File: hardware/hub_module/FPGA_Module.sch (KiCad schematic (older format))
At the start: 1 part, among them U1 TE0714

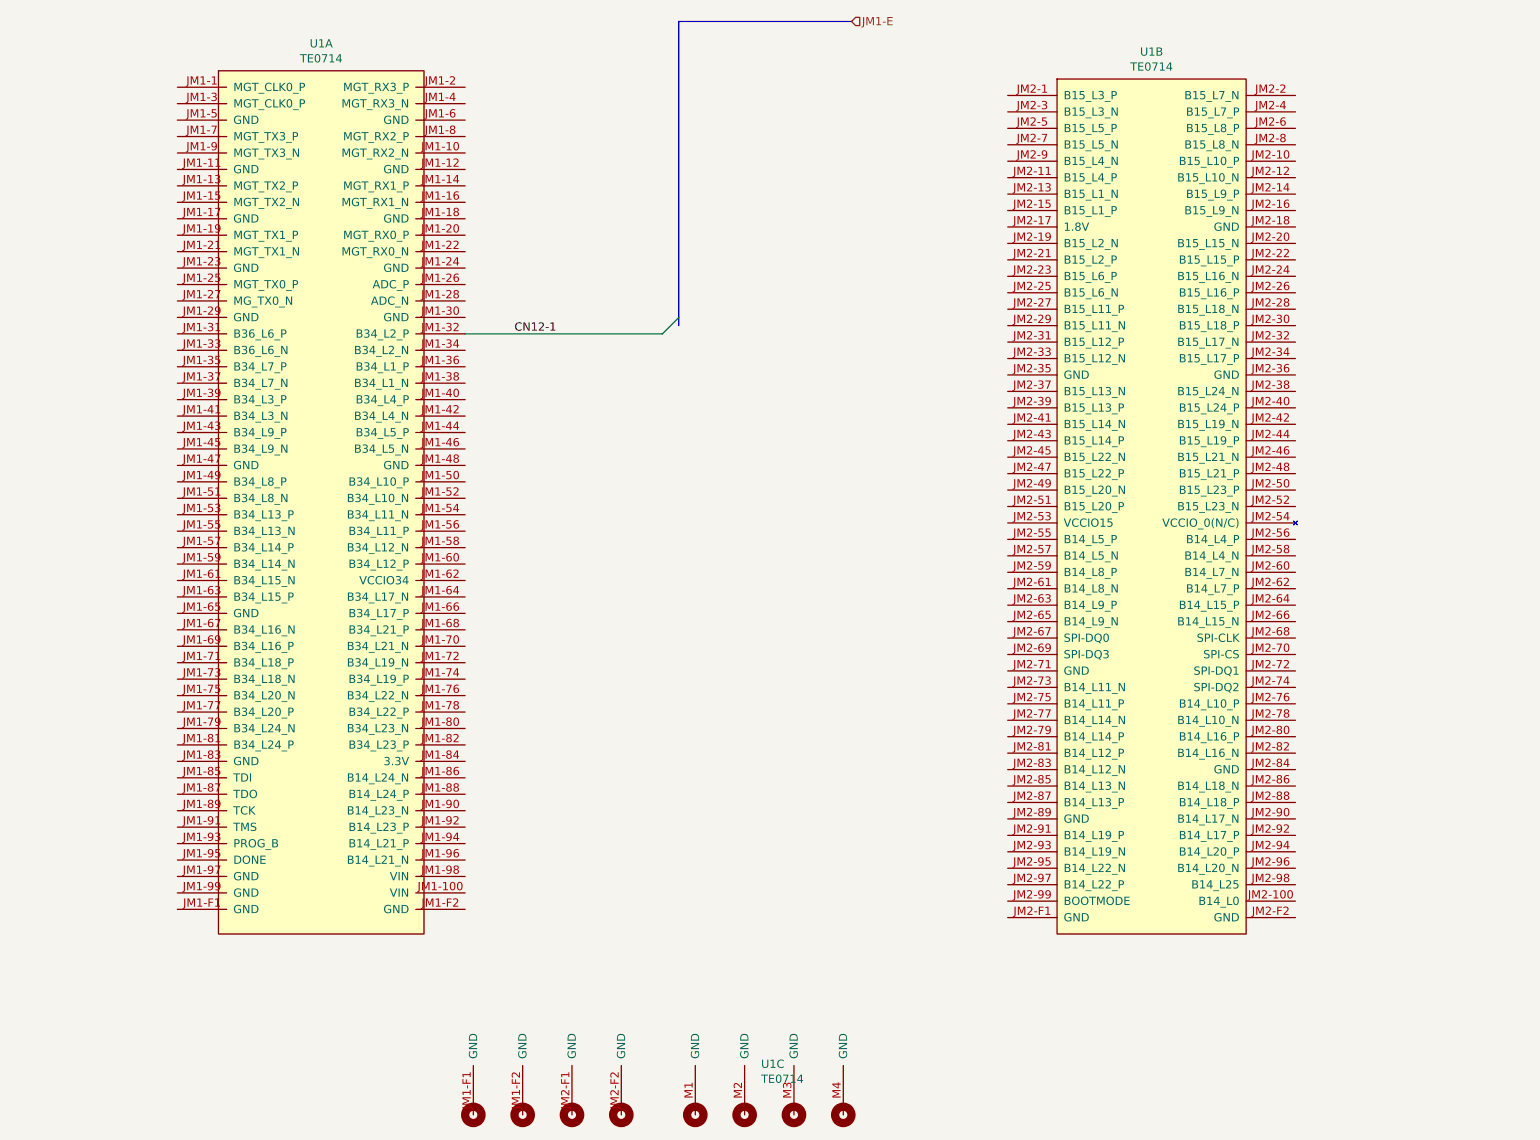
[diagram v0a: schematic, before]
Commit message: busses added
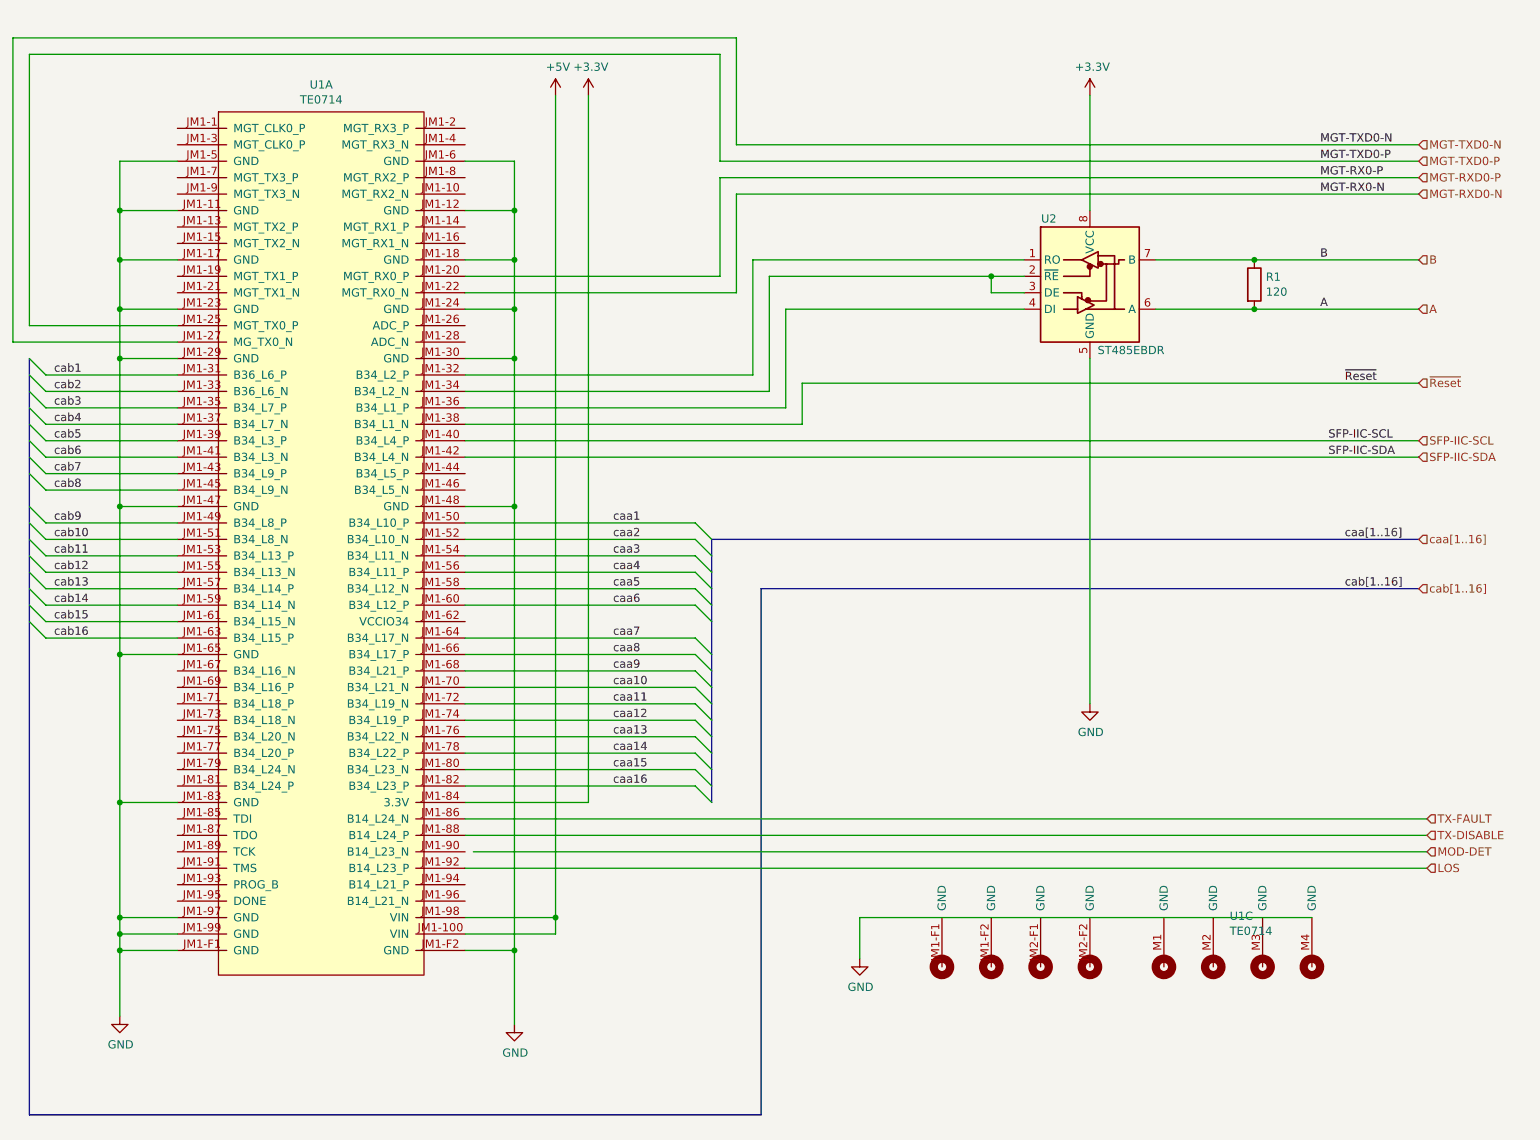
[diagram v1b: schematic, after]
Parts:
- removed unit 2 of U1
- added R1: 120, Resistor_SMD:R_0603_1608Metric, symbol Device:R
- added U2: ST485EBDR, Package_SO:SOIC-8_3.9x4.9mm_P1.27mm, symbol Interface_UART:ST485EBDR
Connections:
- net +5V: now reaches U1.JM1-100 (VIN)
- net +5V: now also U1.JM1-98 (VIN)
- net GND: now reaches U1.JM1-11 (GND)
- net GND: now also U1.JM1-12 (GND), U1.JM1-17 (GND), U1.JM1-18 (GND), U1.JM1-23 (GND), U1.JM1-24 (GND), U1.JM1-29 (GND), U1.JM1-30 (GND), U1.JM1-47 (GND), U1.JM1-48 (GND), U1.JM1-5 (GND), U1.JM1-6 (GND), U1.JM1-65 (GND), U1.JM1-83 (GND), U1.JM1-97 (GND), U1.JM1-99 (GND), U1.JM1-F1 (GND), U1.JM1-F2 (GND), U2.5 (GND)
- net MGT-RXD0-P: now reaches U1.JM1-20 (MGT_RX0_P)
- net MGT-RXD0-N: now reaches U1.JM1-22 (MGT_RX0_N)
- net MGT-TXD0-P: now reaches U1.JM1-25 (MGT_TX0_P)
- net MGT-TXD0-N: now reaches U1.JM1-27 (MG_TX0_N)
- net cab1: now reaches U1.JM1-31 (B36_L6_P)
- net cab2: now reaches U1.JM1-33 (B36_L6_N)
- net at U1.JM1-34 (B34_L2_N): now also U2.2 (~RE), U2.3 (DE)
- net cab3: now reaches U1.JM1-35 (B34_L7_P)
- net at U1.JM1-36 (B34_L1_P): now also U2.4 (DI)
- net cab4: now reaches U1.JM1-37 (B34_L7_N)
- net ~Reset: now reaches U1.JM1-38 (B34_L1_N)
- net cab5: now reaches U1.JM1-39 (B34_L3_P)
- net SFP-IIC-SCL: now reaches U1.JM1-40 (B34_L4_P)
- net cab6: now reaches U1.JM1-41 (B34_L3_N)
- net SFP-IIC-SDA: now reaches U1.JM1-42 (B34_L4_N)
- net cab7: now reaches U1.JM1-43 (B34_L9_P)
- net cab8: now reaches U1.JM1-45 (B34_L9_N)
- net cab9: now reaches U1.JM1-49 (B34_L8_P)
- net caa1: now reaches U1.JM1-50 (B34_L10_P)
- net cab10: now reaches U1.JM1-51 (B34_L8_N)
- net caa2: now reaches U1.JM1-52 (B34_L10_N)
- net cab11: now reaches U1.JM1-53 (B34_L13_P)
- net caa3: now reaches U1.JM1-54 (B34_L11_N)
- net cab12: now reaches U1.JM1-55 (B34_L13_N)
- net caa4: now reaches U1.JM1-56 (B34_L11_P)
- net cab13: now reaches U1.JM1-57 (B34_L14_P)
- net caa5: now reaches U1.JM1-58 (B34_L12_N)
- net cab14: now reaches U1.JM1-59 (B34_L14_N)
- net caa6: now reaches U1.JM1-60 (B34_L12_P)
- net cab15: now reaches U1.JM1-61 (B34_L15_N)
- net cab16: now reaches U1.JM1-63 (B34_L15_P)
- net caa7: now reaches U1.JM1-64 (B34_L17_N)
- net caa8: now reaches U1.JM1-66 (B34_L17_P)
- net caa9: now reaches U1.JM1-68 (B34_L21_P)
- net caa10: now reaches U1.JM1-70 (B34_L21_N)
- net caa11: now reaches U1.JM1-72 (B34_L19_N)
- net caa12: now reaches U1.JM1-74 (B34_L19_P)
- net caa13: now reaches U1.JM1-76 (B34_L22_N)
- net caa14: now reaches U1.JM1-78 (B34_L22_P)
- net caa15: now reaches U1.JM1-80 (B34_L23_N)
- net caa16: now reaches U1.JM1-82 (B34_L23_P)
- net +3V3: now reaches U1.JM1-84 (3.3V)
- net +3V3: now also U2.8 (VCC)
- net TX-FAULT: now reaches U1.JM1-86 (B14_L24_N)
- net TX-DISABLE: now reaches U1.JM1-88 (B14_L24_P)
- net LOS: now reaches U1.JM1-92 (B14_L23_P)
- net CN12-1: no longer names the net of U1.JM1-32 (B34_L2_P)
- net CN12-1: now also U2.1 (RO)
- new net A: R1.2, U2.6 (A)
- new net B: R1.1, U2.7 (B)
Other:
- moved on the sheet: U1A, U1C
